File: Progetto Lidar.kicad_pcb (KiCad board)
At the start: 2 copper layers, 130 x 77 mm, 44 parts, among them J1 CONN_LASER, J10 Conn_01x08, J2 CONN_RICEVITORE, J3 Conn_02x18_Odd_Even, J4 Conn_01x10, J5 Conn_01x08, J6 Conn_01x08, J7 Conn_01x08, J8 Conn_SPI, J9 Conn_01x08

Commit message: Ulteriori modifiche
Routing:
- net GND: vias 10 -> 12
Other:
- board text added: "V1.3 15/04/2025"
- board text removed: "V1.1 25/03/2025"
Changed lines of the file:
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@@
     (fp_arc (start 17.272 53.594) (mid 15.24 54.254237) (end 13.208 53.594) (layer "F.CrtYd") (width 0.15))
     (fp_arc (start 94.488 -0.254) (mid 96.52 -0.914237) (end 98.552 -0.254) (layer "F.CrtYd") (width 0.15))
-    (fp_arc (start 99.314 0.508) (mid 99.650922 1.077974) (end 99.8728 1.7018) (layer "F.CrtYd") (width 0.15))
+    (fp_arc (start 99.314 0.508) (mid 99.650926 1.077973) (end 99.8728 1.7018) (layer "F.CrtYd") (width 0.15))
     (fp_arc (start 92.202 53.594) (mid 90.17 54.254237) (end 88.138 53.594) (layer "F.CrtYd") (width 0.15))
     (fp_circle (center 66.04 35.56) (end 69.24 35.56) (layer "B.Fab") (width 0.15) (fill none))
@@
     (effects (font (size 1 1) (thickness 0.15)))
   )
-  (gr_text "V1.1  25/03/2025" (at 106.426 86.614 90) (layer "F.SilkS")
+  (gr_text "V1.3  15/04/2025" (at 106.426 86.614 90) (layer "F.SilkS")
     (effects (font (size 1 1) (thickness 0.15)))
   )
@@
   (segment (start 160.854065 64.256065) (end 160.86 64.262) (width 0.25) (layer "F.Cu") (net 67))
   (segment (start 160.854065 57.372981) (end 160.854065 64.256065) (width 0.25) (layer "F.Cu") (net 67))
-  (segment (start 187.551 92.657503) (end 187.551 90.723502) (width 1) (layer "F.Cu") (net 68))
   (segment (start 100.916 112.522) (end 100.916 112.444) (width 1) (layer "F.Cu") (net 68))
   (segment (start 102.87 110.49) (end 133.35 110.49) (width 1) (layer "F.Cu") (net 68))
   (segment (start 203.2 89.662) (end 203.2 86.106) (width 0.5) (layer "F.Cu") (net 68))
+  (segment (start 187.551 91.031) (end 184.912 88.392) (width 1) (layer "F.Cu") (net 68))
   (segment (start 193.614 71.374) (end 193.6515 71.3365) (width 0.5) (layer "F.Cu") (net 68))
   (segment (start 182.232 53.982) (end 183.134 54.884) (width 0.5) (layer "F.Cu") (net 68))
   (segment (start 168.48 69.342) (end 165.686 72.136) (width 1) (layer "F.Cu") (net 68))
-  (segment (start 188.976 93.914) (end 188.807497 93.914) (width 1) (layer "F.Cu") (net 68))
+  (segment (start 187.551 92.657503) (end 187.551 91.031) (width 1) (layer "F.Cu") (net 68))
   (segment (start 188.976 93.914) (end 191.008 93.914) (width 1) (layer "F.Cu") (net 68))
   (segment (start 183.388 57.55) (end 182.934 57.096) (width 0.5) (layer "F.Cu") (net 68))
@@
   (segment (start 191.008 93.914) (end 192.344 93.914) (width 1) (layer "F.Cu") (net 68))
   (segment (start 202.372 90.932) (end 202.372 90.49) (width 0.5) (layer "F.Cu") (net 68))
-  (segment (start 187.551 90.723502) (end 185.232 88.404502) (width 1) (layer "F.Cu") (net 68))
   (segment (start 194.88 96.55595) (end 194.88 94.992) (width 0.5) (layer "F.Cu") (net 68))
   (segment (start 100.916 112.522) (end 100.916 118.799) (width 1) (layer "F.Cu") (net 68))
@@
   (segment (start 203.2 86.106) (end 202.926 86.38) (width 0.5) (layer "F.Cu") (net 68))
   (segment (start 97.297 58.4) (end 97.297 61.991) (width 1) (layer "F.Cu") (net 68))
+  (segment (start 184.912 71.882) (end 182.372 69.342) (width 1) (layer "F.Cu") (net 68))
   (segment (start 202.0805 77.216) (end 201.93 77.0655) (width 0.25) (layer "F.Cu") (net 68))
   (segment (start 117.68 56.934) (end 117.617 56.871) (width 1) (layer "F.Cu") (net 68))
@@
   (segment (start 202.372 90.932) (end 202.372 92.964) (width 0.5) (layer "F.Cu") (net 68))
   (segment (start 193.6515 69.342) (end 193.6515 68.4765) (width 0.5) (layer "F.Cu") (net 68))
-  (segment (start 185.232 72.202) (end 182.372 69.342) (width 1) (layer "F.Cu") (net 68))
+  (segment (start 184.912 88.392) (end 184.912 71.882) (width 1) (layer "F.Cu") (net 68))
   (segment (start 197.678 102.362) (end 197.612 102.296) (width 0.5) (layer "F.Cu") (net 68))
   (segment (start 197.678 74.138) (end 197.678 75.184) (width 0.5) (layer "F.Cu") (net 68))
@@
   (segment (start 196.088 66.04) (end 198.2235 66.04) (width 0.5) (layer "F.Cu") (net 68))
   (segment (start 197.932 109.54) (end 200.976 112.584) (width 0.25) (layer "F.Cu") (net 68))
+  (segment (start 188.807497 93.914) (end 187.551 92.657503) (width 1) (layer "F.Cu") (net 68))
+  (segment (start 188.976 93.914) (end 188.807497 93.914) (width 1) (layer "F.Cu") (net 68))
   (segment (start 192.344 93.914) (end 193.802 93.914) (width 1) (layer "F.Cu") (net 68))
   (segment (start 145.288 87.122) (end 140.667 87.122) (width 1) (layer "F.Cu") (net 68))
   (segment (start 181.9425 64.6915) (end 183.388 63.246) (width 0.5) (layer "F.Cu") (net 68))
-  (segment (start 188.807497 93.914) (end 187.551 92.657503) (width 1) (layer "F.Cu") (net 68))
   (segment (start 148.59 95.25) (end 148.59 90.424) (width 1) (layer "F.Cu") (net 68))
   (segment (start 183.134 56.896) (end 182.934 57.096) (width 0.5) (layer "F.Cu") (net 68))
@@
   (segment (start 184.396 53.982) (end 182.232 53.982) (width 0.5) (layer "F.Cu") (net 68))
   (segment (start 202.079 75.079) (end 203.944 73.214) (width 0.5) (layer "F.Cu") (net 68))
-  (segment (start 185.232 88.404502) (end 185.232 72.202) (width 1) (layer "F.Cu") (net 68))
   (segment (start 179.832 69.342) (end 182.372 69.342) (width 1) (layer "F.Cu") (net 68))
   (segment (start 171.02 69.342) (end 179.832 69.342) (width 1) (layer "F.Cu") (net 68))
@@
   (via (at 198.374 85.852) (size 0.6) (drill 0.3) (layers "F.Cu" "B.Cu") (net 68))
   (via (at 161.544 98.298) (size 0.6) (drill 0.3) (layers "F.Cu" "B.Cu") (free) (net 68))
+  (via (at 184.658 92.202) (size 0.6) (drill 0.3) (layers "F.Cu" "B.Cu") (free) (net 68))
   (via (at 164.846 96.52) (size 0.6) (drill 0.3) (layers "F.Cu" "B.Cu") (free) (net 68))
   (via (at 158.496 84.074) (size 0.6) (drill 0.3) (layers "F.Cu" "B.Cu") (free) (net 68))
   (via (at 192.344 93.914) (size 0.8) (drill 0.4) (layers "F.Cu" "B.Cu") (net 68))
+  (via (at 184.658 89.662) (size 0.6) (drill 0.3) (layers "F.Cu" "B.Cu") (free) (net 68))
   (segment (start 203.944 73.214) (end 203.944 64.454) (width 1) (layer "B.Cu") (net 68))
   (segment (start 192.344 96.332) (end 199.836 103.824) (width 1) (layer "B.Cu") (net 68))

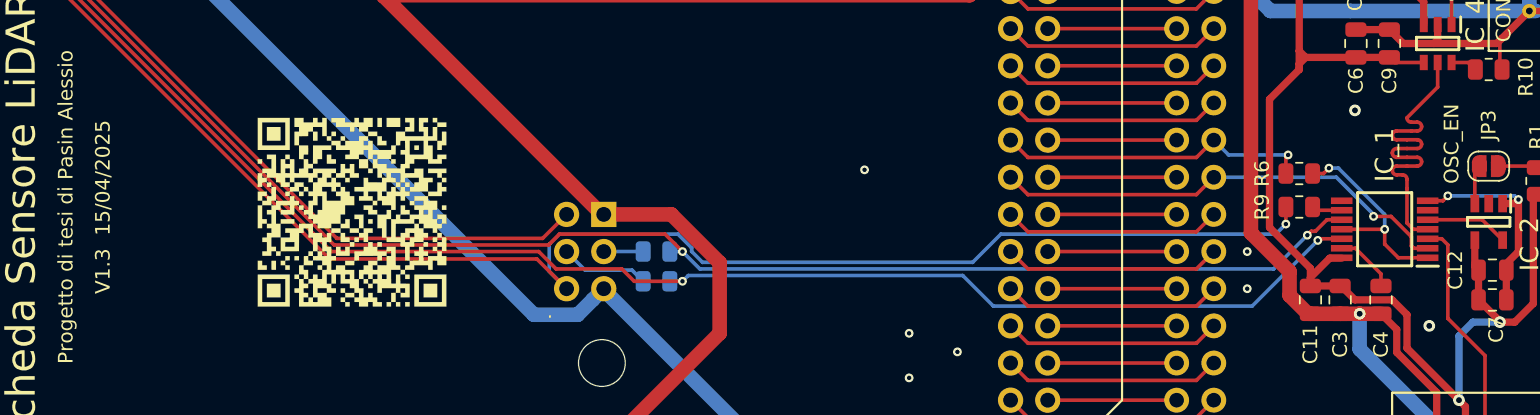
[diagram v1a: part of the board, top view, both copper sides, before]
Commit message: Corretto collegamento TDC_START
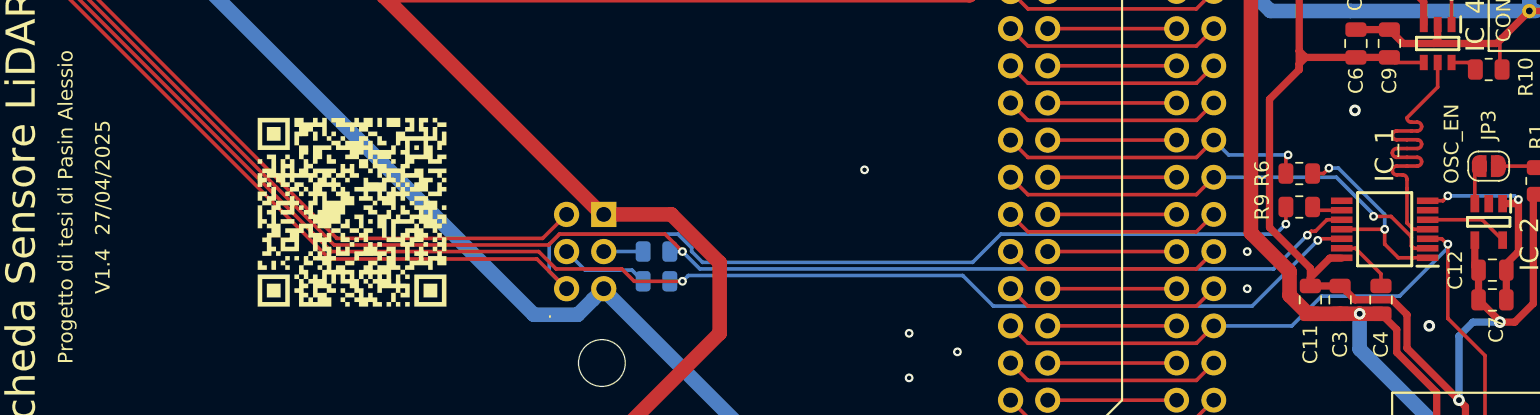
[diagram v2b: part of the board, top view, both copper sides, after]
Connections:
- IC_0 pad D34: /ARD_GPIO_D34 -> /TDC_START
- J3 pad 15: /ARD_GPIO_D34 -> /TDC_START
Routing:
- net /TDC_START: track 23.4 -> 56.7 mm, vias 0 -> 1
- net /ARD_GPIO_D34: track 14.9 -> 0.00 mm
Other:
- board text added: "V1.4 27/04/2025"
- board text removed: "V1.3 15/04/2025"

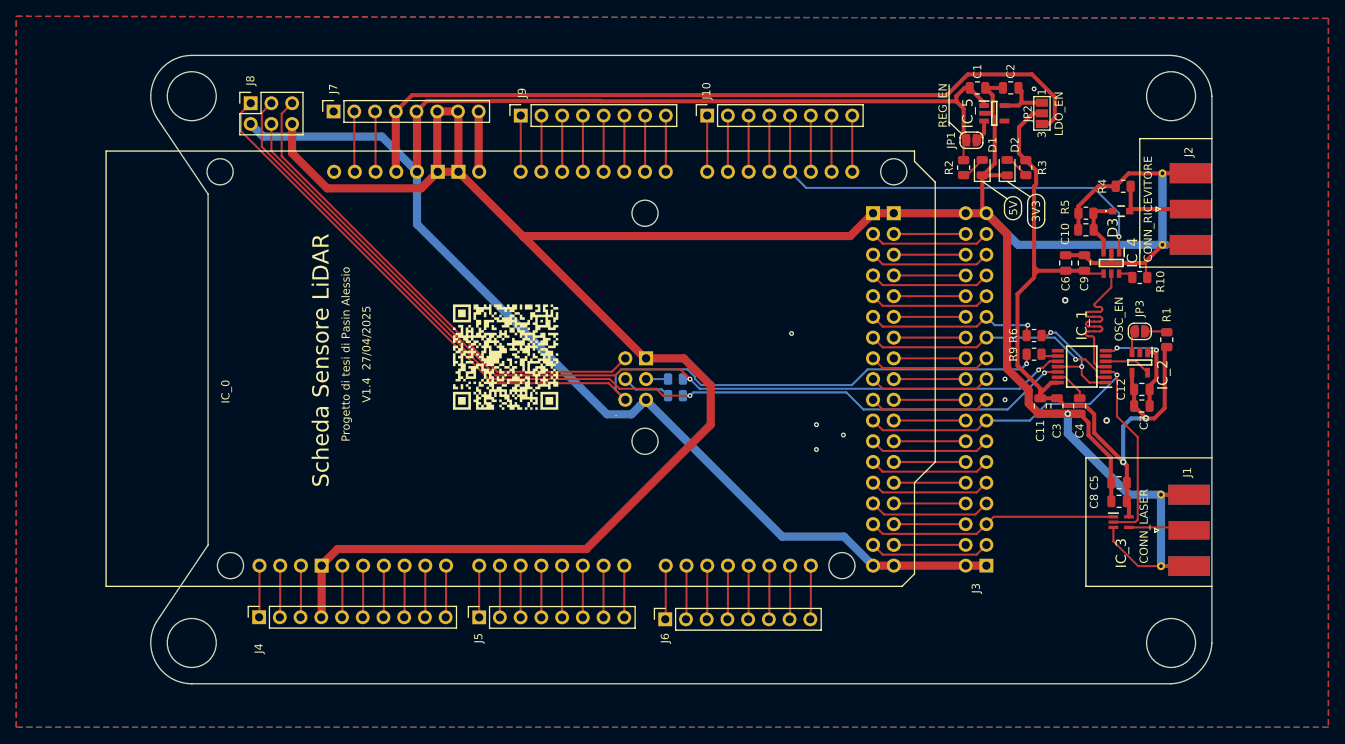
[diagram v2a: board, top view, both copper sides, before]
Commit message: Aggiunto vias nei circuiti veloci, rimosso piste GND, organizzato cartella e file, generato i file per la produzione
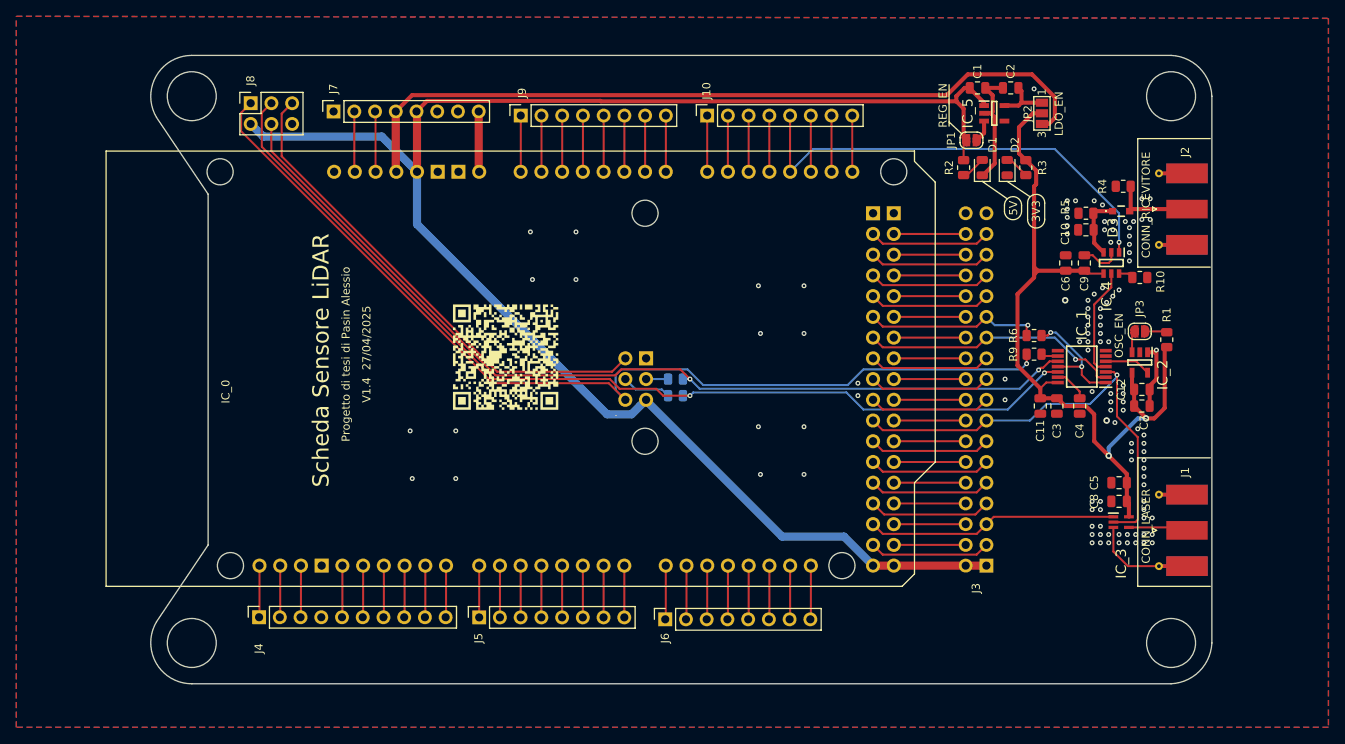
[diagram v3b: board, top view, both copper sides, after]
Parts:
- moved J2 0.43 mm to (205.2, 68.8)
- moved J1 0.25 mm to (205.2, 108.2)
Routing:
- net GND: track 390.7 -> 37.5 mm, vias 12 -> 113
- net /TDC_STOP: track 23.5 -> 13.4 mm
- net /ARD_V_REF: track 54.1 -> 56.4 mm
- net +3V3: track 99.0 -> 97.5 mm
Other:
- board text added: "CONN_LASER"
- board text added: "CONN_RICEVITORE"

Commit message: Corretto connessione TDC ENABLE
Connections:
- IC_0 pad D38: /ARD_GPIO_D38 -> /TDC_EN
- IC_1 pad 1: /SPI_CS -> /TDC_EN
- J3 pad 19: /ARD_GPIO_D38 -> /TDC_EN
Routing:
- net /TDC_EN: track 0.00 -> 31.1 mm, vias 0 -> 1
- net /ARD_GPIO_D38: track 14.9 -> 0.00 mm
- net /SPI_CS: track 14.7 -> 10.3 mm
- net GND: vias 113 -> 114

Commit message: Rifatti i file per la produzione, modificato diametro fori, aggiunto scritte sul retro
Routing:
- net (no net): track 0.00 -> 0.51 mm
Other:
- outline, holes or cut-outs redrawn
- board text added: "V1.5 13/05/2025"
- board text removed: "V1.4 27/04/2025"
